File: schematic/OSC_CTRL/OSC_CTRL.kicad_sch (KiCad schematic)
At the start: 14 parts, among them SW1 SW_DIP_x08, SW2 SW_DIP_x08, U1 4052, U2 74AHC595

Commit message: sending ACM v1 rev 1 and APM v5 rev 1 out
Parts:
- removed RV1, RV2, RV3, RV4: R_Potentiometer, Potentiometer_THT:Potentiometer_Bourns_PTA4543_Single_Slide, symbol Device:R_Potentiometer
- removed RV5: 250k, Potentiometer_THT:Potentiometer_Piher_T-16H_Single_Horizontal, symbol Device:R_Potentiometer
- removed SW1: SW_DIP_x08, symbol Switch:SW_DIP_x08
- added D1: 1N5819, Diode_THT:D_DO-41_SOD81_P10.16mm_Horizontal, symbol Diode:1N5819
- added RV11, RV12, RV13, RV14: 10K, Potentiometer_THT:Potentiometer_Bourns_PTA4543_Single_Slide, symbol Device:R_Potentiometer
- added RV15: 250K, Potentiometer_THT:Potentiometer_Piher_T-16H_Single_Horizontal, symbol Device:R_Potentiometer
- added SW3: SW_DIP_x08, symbol Switch:SW_DIP_x08
- RV6, RV7, RV8, RV9: value R_Potentiometer -> 10K
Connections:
- net 3V3: now also RV10.1, RV6.1, RV7.1, RV8.1, RV9.1, RV11.1, RV12.1, RV13.1, RV14.1, RV15.1
- net GND: now also RV10.3, RV6.3, RV7.3, RV8.3, RV9.3, RV11.3, RV12.3, RV13.3, RV14.3, RV15.3
- net OSC1_WAVE0: now also SW3.1
- net OSC1_WAVE1: now also SW3.2
- net OSC1_WAVE2: now also SW3.3
- net OSC_1_ATK: now also RV11.2
- net OSC_1_DEC: now also RV12.2
- net OSC_1_REL: now also U1.15 (X2), RV14.2; no longer U1.11 (X3)
- net OSC_1_SUS: now also U1.11 (X3), RV13.2; no longer U1.15 (X2)
- net OSC_2_ATK: now also RV6.2
- net OSC_2_DEC: now also RV7.2
- net OSC_2_REL: now also RV9.2, U1.2 (Y2); no longer U1.4 (Y3)
- net OSC_2_SUS: now also RV8.2, U1.4 (Y3); no longer U1.2 (Y2)
- net STM32_ADC_15: now also RV15.2
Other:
- note added: "OSCILLATOR 1"
- note added: "OSCILLATOR 2"
- note added: "WAVEFORM SELECT"
- note removed: "OSCILLATOR A"
- note removed: "OSCILLATOR B"
- moved on the sheet: RV10, RV6, RV7, RV8, RV9, SW2, U1, U2

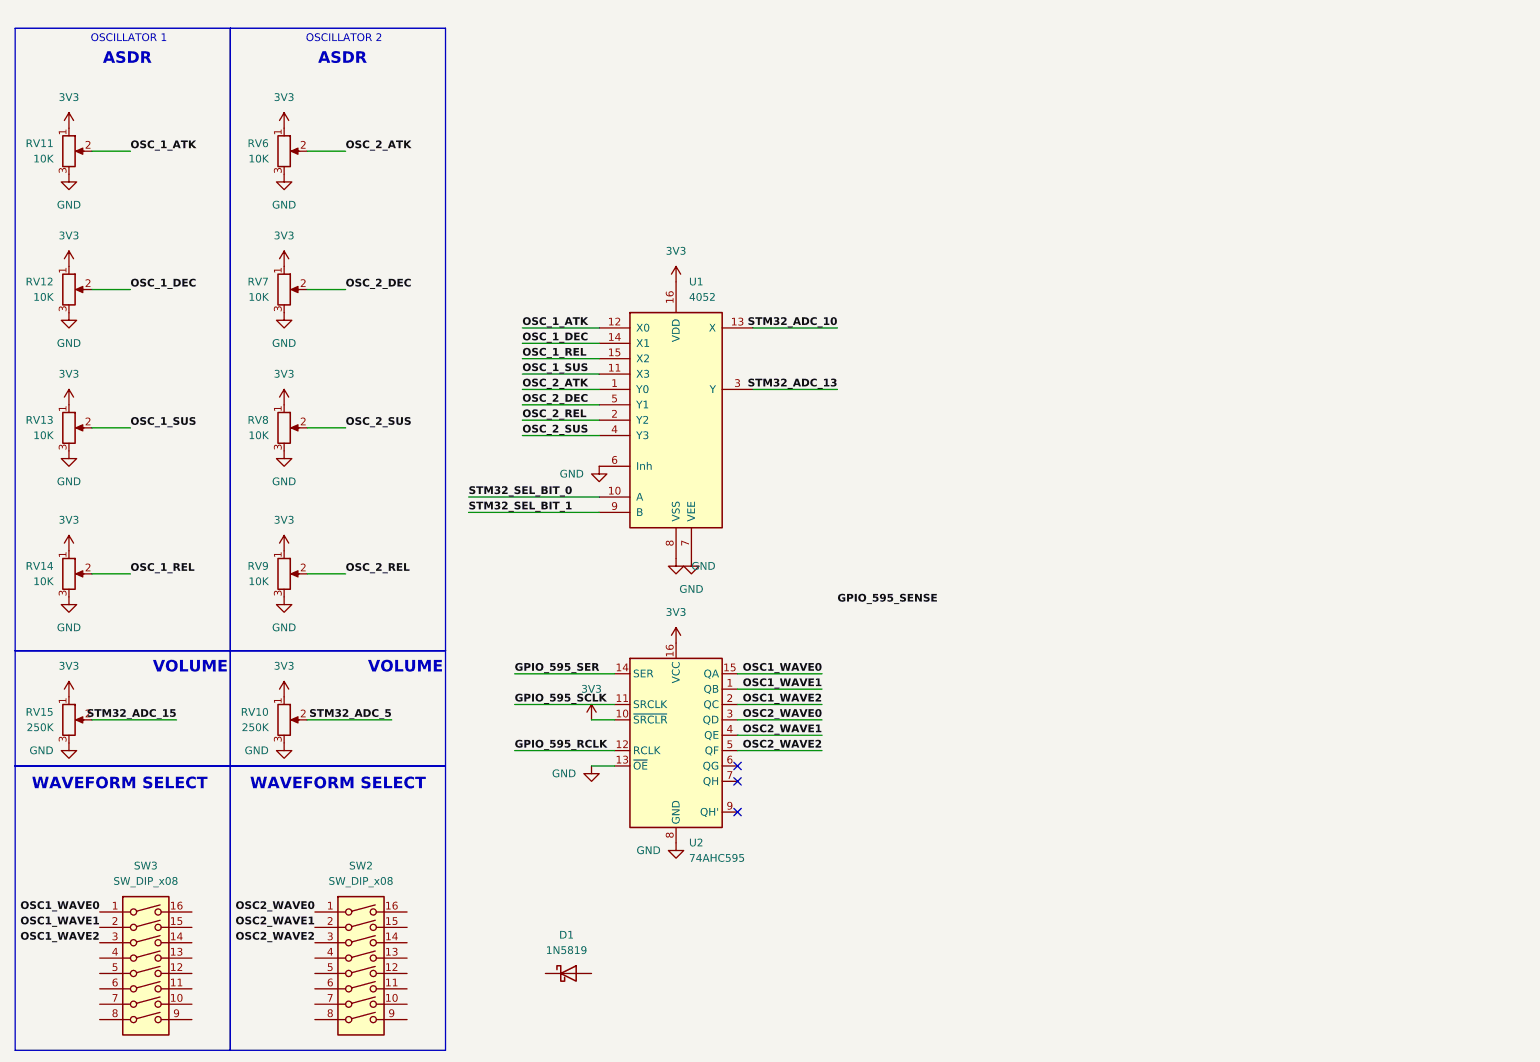
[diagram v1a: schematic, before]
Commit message: starting pcb for oscillator ctrl board
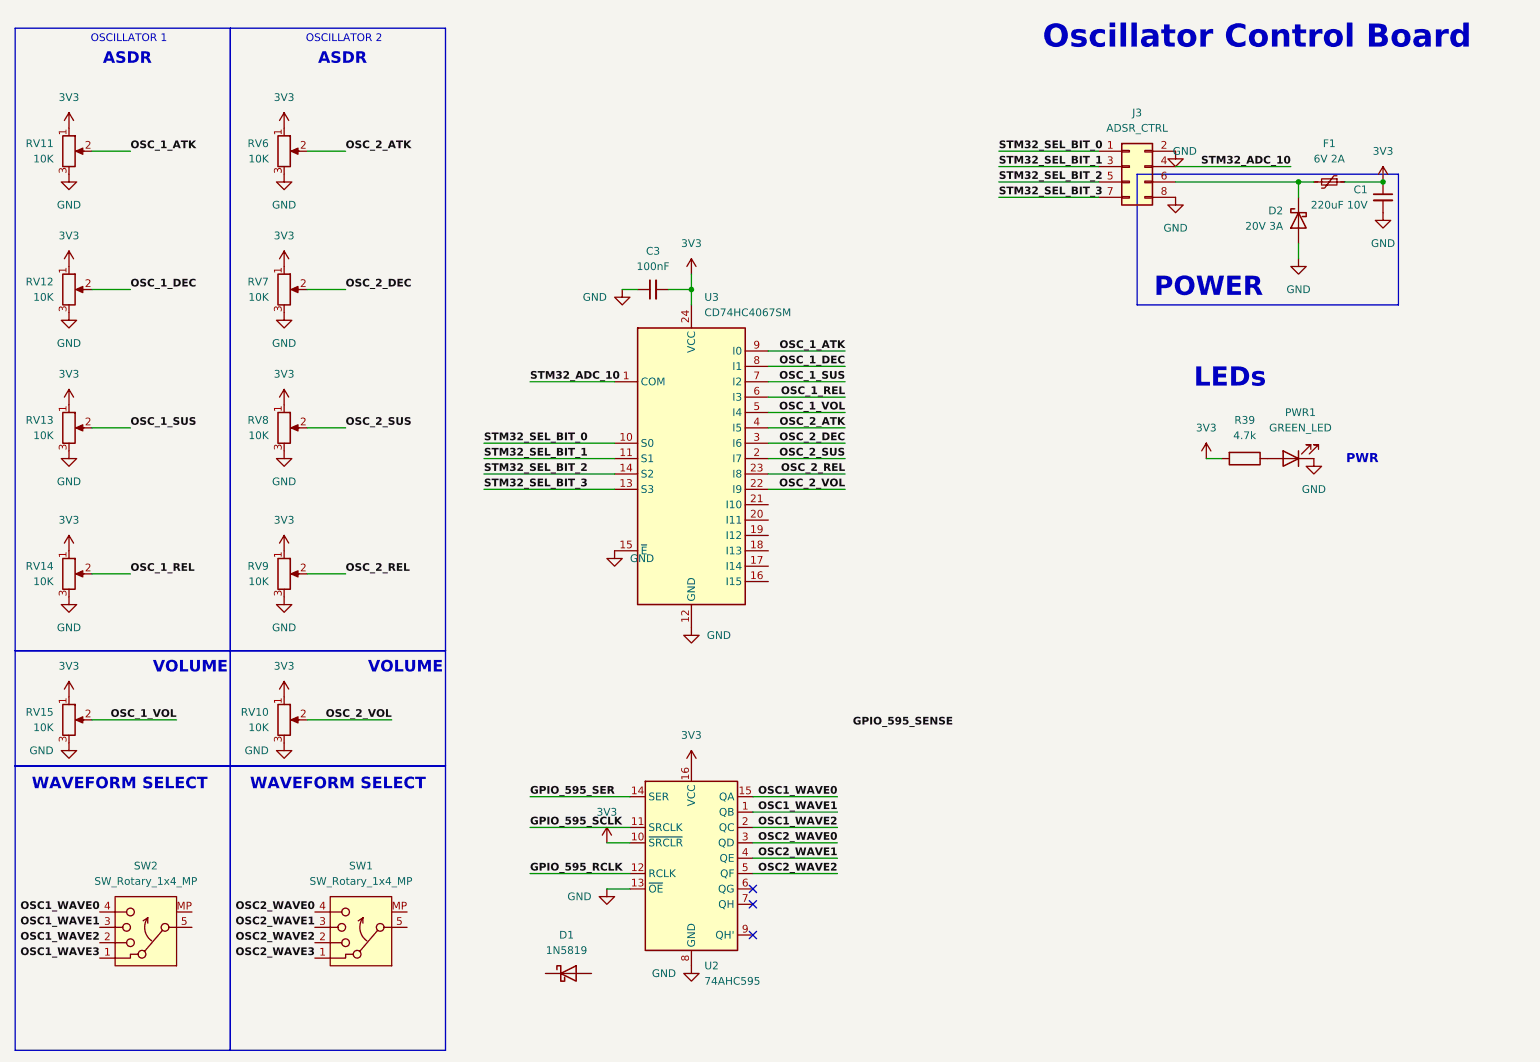
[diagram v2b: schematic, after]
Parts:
- removed SW2, SW3: SW_DIP_x08, symbol Switch:SW_DIP_x08
- removed U1: 4052, symbol 4xxx:4052
- added C1: 220uF 10V, Capacitor_SMD:CP_Elec_4x3, symbol Device:C_Small
- added C3: 100nF, Capacitor_SMD:C_0402_1005Metric, symbol Device:C_Small
- added D2: 20V 3A, Diode_SMD:D_SOD-123, symbol Device:D_Schottky
- added F1: 6V 2A, Fuse:Fuse_0603_1608Metric, symbol Device:Polyfuse_Small
- added J3: ADSR_CTRL, Connector_PinHeader_2.54mm:PinHeader_2x04_P2.54mm_Vertical_SMD, symbol Connector_Generic:Conn_02x04_Odd_Even
- added PWR1: GREEN_LED, LED_SMD:LED_0603_1608Metric, symbol Device:LED
- added R39: 4.7k, Resistor_SMD:R_0201_0603Metric, symbol Device:R
- added SW1, SW2: SW_Rotary_1x4_MP, symbol Switch:SW_Rotary_1x4_MP
- added U3: CD74HC4067SM, Package_SO:SSOP-24_5.3x8.2mm_P0.65mm, symbol 74xx:CD74HC4067SM
- RV10, RV15: value 250K -> 10K
- U2: footprint (none) -> Package_DIP:DIP-16_W7.62mm_SMDSocket_SmallPads
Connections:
- net 3V3: now also C1.1, C3.2, F1.1, R39.2, U3.24 (VCC)
- net GND: now also C1.2, C3.1, D2.2 (A), J3.2 (Pin_2), J3.8 (Pin_8), PWR1.1 (K), U3.12 (GND), U3.15 (~{E})
- net OSC1_WAVE0: now also SW2.4
- net OSC1_WAVE1: now also SW2.3
- net OSC1_WAVE2: now also SW2.2
- net OSC2_WAVE0: now also SW1.4
- net OSC2_WAVE1: now also SW1.3
- net OSC2_WAVE2: now also SW1.2
- net OSC_1_ATK: now also U3.9 (I0)
- net OSC_1_DEC: now also U3.8 (I1)
- net OSC_1_REL: now also U3.6 (I3)
- net OSC_1_SUS: now also U3.7 (I2)
- net OSC_2_ATK: now also U3.4 (I5)
- net OSC_2_DEC: now also U3.3 (I6)
- net OSC_2_REL: now also U3.23 (I8)
- net OSC_2_SUS: now also U3.2 (I7)
- net STM32_ADC_10: now also J3.4 (Pin_4), U3.1 (COM)
- net STM32_SEL_BIT_0: now also J3.1 (Pin_1), U3.10 (S0)
- net STM32_SEL_BIT_1: now also J3.3 (Pin_3), U3.11 (S1)
- net STM32_ADC_15 renamed OSC_1_VOL
- net OSC_1_VOL: now also U3.5 (I4)
- net STM32_ADC_5 renamed OSC_2_VOL
- net OSC_2_VOL: now also U3.22 (I9)
- new net: D2.1 (K), F1.2, J3.6 (Pin_6)
- new net: PWR1.2 (A), R39.1
- new net OSC1_WAVE3: SW2.1
- new net OSC2_WAVE3: SW1.1
- new net STM32_SEL_BIT_2: J3.5 (Pin_5), U3.14 (S2)
- new net STM32_SEL_BIT_3: J3.7 (Pin_7), U3.13 (S3)
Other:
- note added: "LEDs"
- note added: "Oscillator Control Board"
- note added: "POWER"
- note added: "PWR"
- moved on the sheet: U2

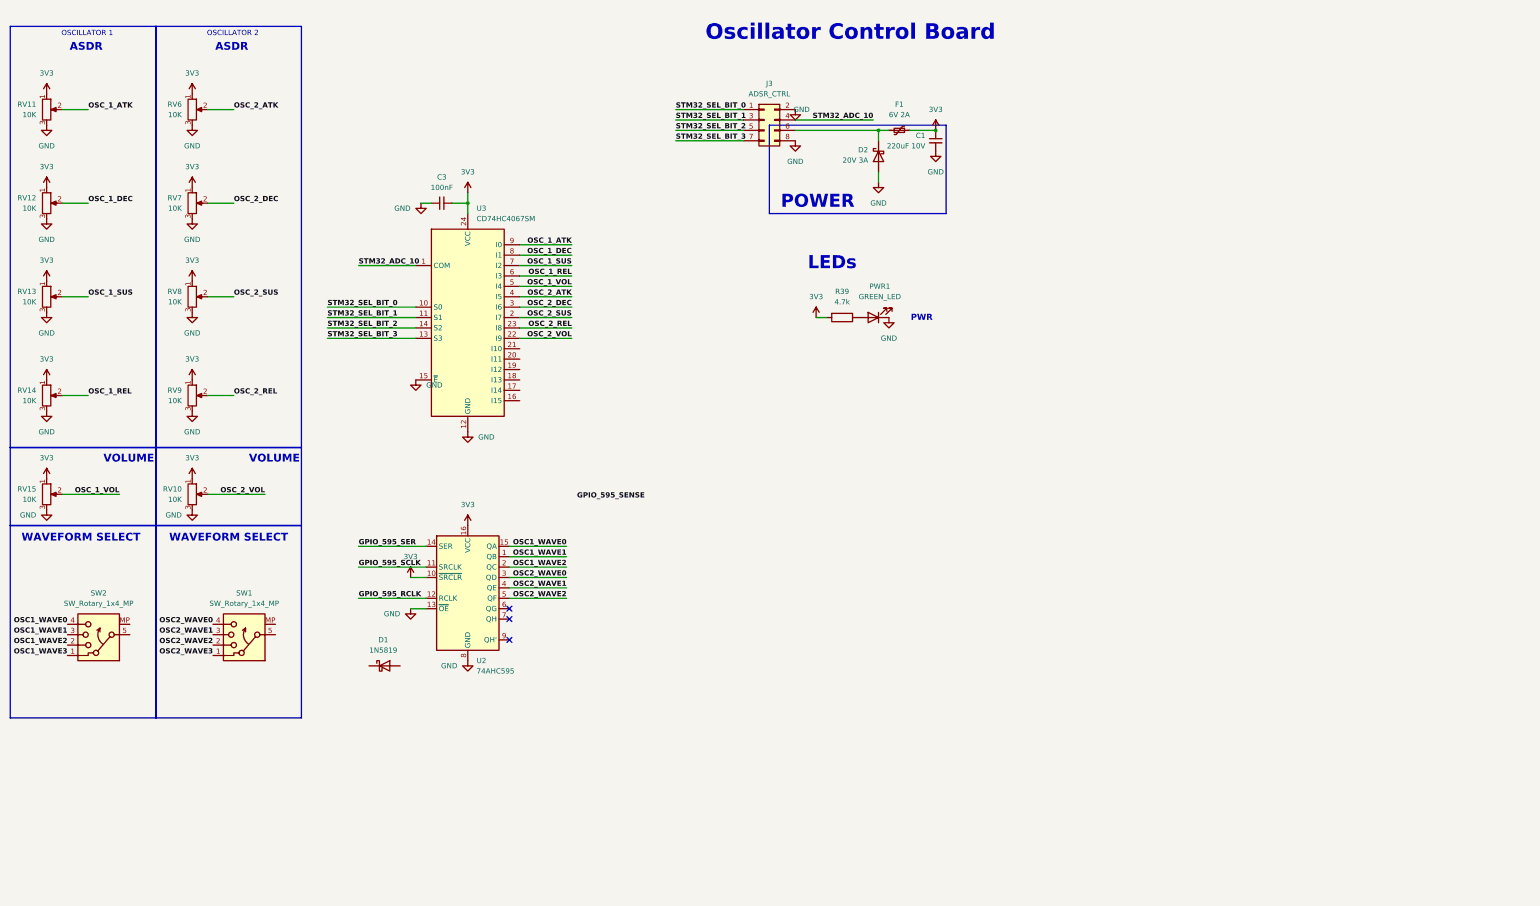
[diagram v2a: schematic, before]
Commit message: oscillator control board sent out
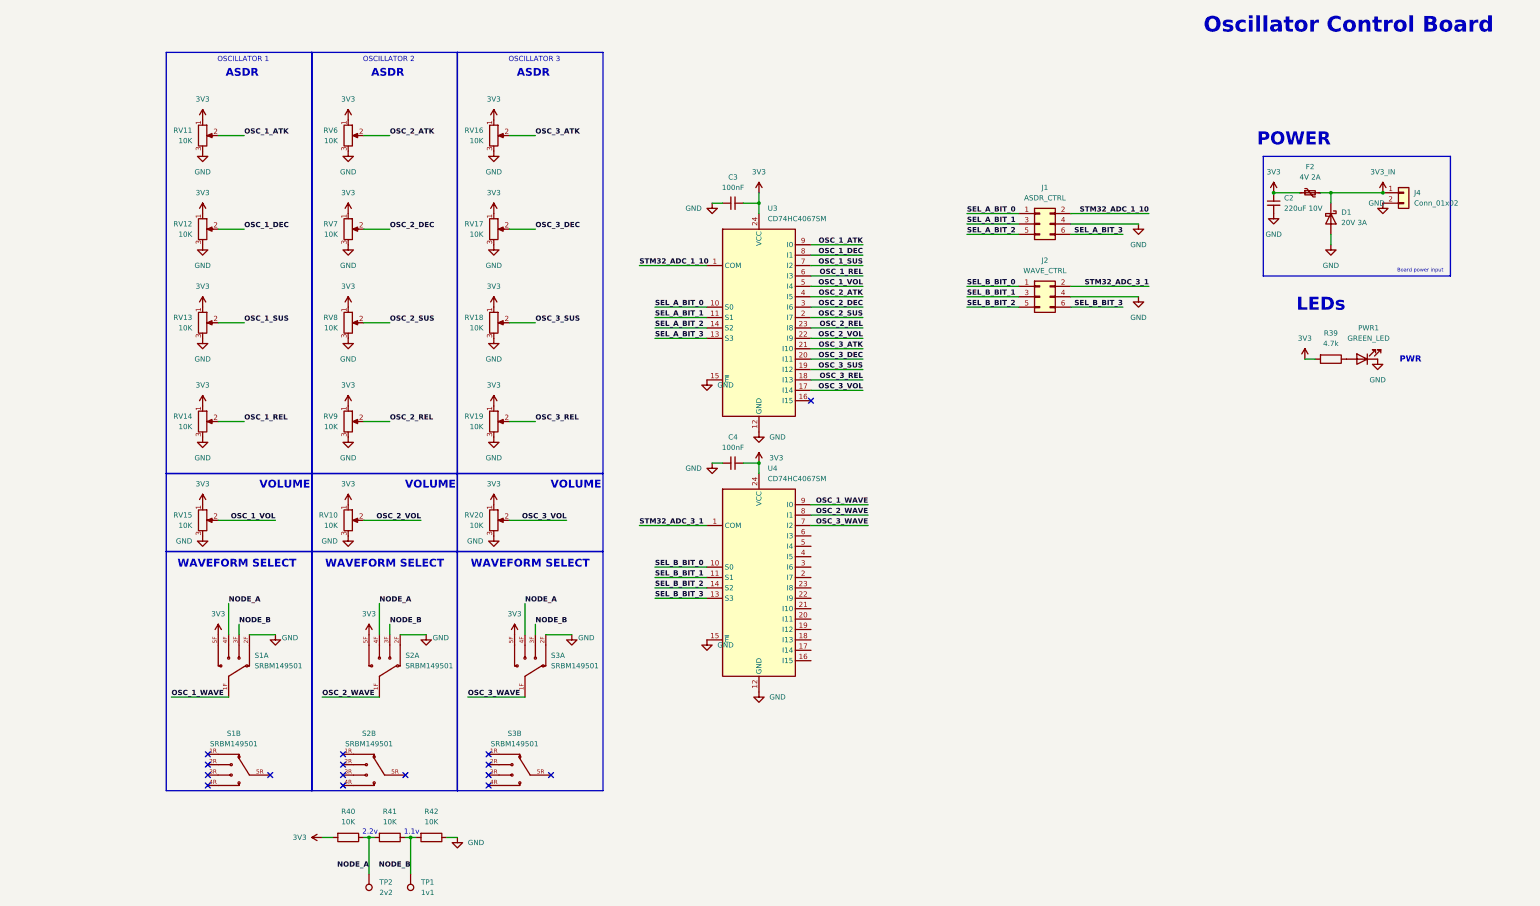
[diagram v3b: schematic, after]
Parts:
- removed C1: 220uF 10V, Capacitor_SMD:CP_Elec_4x3, symbol Device:C_Small
- removed D1: 1N5819, Diode_THT:D_DO-41_SOD81_P10.16mm_Horizontal, symbol Diode:1N5819
- removed D2: 20V 3A, Diode_SMD:D_SOD-123, symbol Device:D_Schottky
- removed F1: 6V 2A, Fuse:Fuse_0603_1608Metric, symbol Device:Polyfuse_Small
- removed J3: ADSR_CTRL, Connector_PinHeader_2.54mm:PinHeader_2x04_P2.54mm_Vertical_SMD, symbol Connector_Generic:Conn_02x04_Odd_Even
- removed SW1, SW2: SW_Rotary_1x4_MP, symbol Switch:SW_Rotary_1x4_MP
- removed U2: 74AHC595, Package_DIP:DIP-16_W7.62mm_SMDSocket_SmallPads, symbol 74xx:74AHC595
- added C2: 220uF 10V, Capacitor_SMD:CP_Elec_4x3, symbol Device:C_Small
- added C4: 100nF, Capacitor_SMD:C_0402_1005Metric, symbol Device:C_Small
- added D1: 20V 3A, Diode_SMD:D_SOD-123, symbol Device:D_Schottky
- added F2: 4V 2A, Fuse:Fuse_0603_1608Metric, symbol Device:Polyfuse_Small
- added J1: ASDR_CTRL, Connector_PinHeader_2.54mm:PinHeader_2x03_P2.54mm_Vertical_SMD, symbol Connector_Generic:Conn_02x03_Odd_Even
- added J2: WAVE_CTRL, Connector_PinHeader_2.54mm:PinHeader_2x03_P2.54mm_Vertical_SMD, symbol Connector_Generic:Conn_02x03_Odd_Even
- added J4: Conn_01x02, Connector_PinSocket_2.54mm:PinSocket_1x02_P2.54mm_Vertical_SMD_Pin1Left, symbol Connector_Generic:Conn_01x02
- added R40, R41, R42: 10K, Resistor_SMD:R_0201_0603Metric, symbol Device:R
- added RV16, RV17, RV18, RV19: 10K, my_footprints:Potentiometer_Bourns_PTA4543_Single_Slide, symbol Device:R_Potentiometer
- added RV20: 10K, my_footprints:Potentiometer_Piher_PC-16_Single_Horizontal, symbol Device:R_Potentiometer
- added S1, S2, S3: SRBM149501, my_footprints:SW_SRBM149501, symbol SRBM149501:SRBM149501
- added TP1: 1v1, TestPoint:TestPoint_Pad_D1.0mm, symbol Connector:TestPoint
- added TP2: 2v2, TestPoint:TestPoint_Pad_D1.0mm, symbol Connector:TestPoint
- added U4: CD74HC4067SM, Package_SO:SSOP-24_5.3x8.2mm_P0.65mm, symbol 74xx:CD74HC4067SM
- RV10: footprint Potentiometer_THT:Potentiometer_Piher_T-16H_Single_Horizontal -> my_footprints:Potentiometer_Piher_PC-16_Single_Horizontal
- RV11, RV12, RV13, RV14, RV6, RV7, RV8, RV9: footprint Potentiometer_THT:Potentiometer_Bourns_PTA4543_Single_Slide -> my_footprints:Potentiometer_Bourns_PTA4543_Single_Slide
- RV15: footprint Potentiometer_THT:Potentiometer_Piher_T-16H_Single_Horizontal -> Potentiometer_THT:Potentiometer_Piher_PC-16_Single_Horizontal
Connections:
- net 3V3: now also C2.1, C4.2, F2.1, R40.2, RV16.1, RV17.1, RV18.1, RV19.1, RV20.1, S1.5F, S2.5F, S3.5F, U4.24 (VCC)
- net GND: now also C2.2, C4.1, D1.2 (A), J1.4 (Pin_4), J2.4 (Pin_4), J4.2 (Pin_2), R42.1, RV16.3, RV17.3, RV18.3, RV19.3, RV20.3, S1.2F, S2.2F, S3.2F, U4.12 (GND), U4.15 (~{E})
- net OSC_3_VOL: now reaches U3.17 (I14)
- net OSC_3_VOL: now also RV20.2
- net OSC_3_REL: now reaches U3.18 (I13)
- net OSC_3_REL: now also RV19.2
- net OSC_3_SUS: now reaches U3.19 (I12)
- net OSC_3_SUS: now also RV18.2
- net OSC_3_DEC: now reaches U3.20 (I11)
- net OSC_3_DEC: now also RV17.2
- net OSC_3_ATK: now reaches U3.21 (I10)
- net OSC_3_ATK: now also RV16.2
- net STM32_ADC_10 renamed STM32_ADC_1_10
- net STM32_ADC_1_10: now also J1.2 (Pin_2)
- net STM32_SEL_BIT_0 renamed SEL_A_BIT_0
- net SEL_A_BIT_0: now also J1.1 (Pin_1)
- net STM32_SEL_BIT_1 renamed SEL_A_BIT_1
- net SEL_A_BIT_1: now also J1.3 (Pin_3)
- net STM32_SEL_BIT_2 renamed SEL_A_BIT_2
- net SEL_A_BIT_2: now also J1.5 (Pin_5)
- net STM32_SEL_BIT_3 renamed SEL_A_BIT_3
- net SEL_A_BIT_3: now also J1.6 (Pin_6)
- new net 3V3_IN: D1.1 (K), F2.2, J4.1 (Pin_1)
- new net NODE_A: R40.1, R41.2, S1.4F, S2.4F, S3.4F, TP2.1
- new net NODE_B: R41.1, R42.2, S1.3F, S2.3F, S3.3F, TP1.1
- new net OSC_1_WAVE: S1.1F, U4.9 (I0)
- new net OSC_2_WAVE: S2.1F, U4.8 (I1)
- new net OSC_3_WAVE: S3.1F, U4.7 (I2)
- new net SEL_B_BIT_0: J2.1 (Pin_1), U4.10 (S0)
- new net SEL_B_BIT_1: J2.3 (Pin_3), U4.11 (S1)
- new net SEL_B_BIT_2: J2.5 (Pin_5), U4.14 (S2)
- new net SEL_B_BIT_3: J2.6 (Pin_6), U4.13 (S3)
- new net STM32_ADC_3_1: J2.2 (Pin_2), U4.1 (COM)
- no-connect marks 3 -> 16
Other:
- note added: "1.1v"
- note added: "2.2v"
- note added: "Board power input"
- note added: "OSCILLATOR 3"
- moved on the sheet: C3, PWR1, R39, RV10, RV11, RV12, RV13, RV14, RV15, RV6, RV7, RV8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

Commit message: getting the boards fabbed
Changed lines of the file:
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@@
 	(wire
 		(pts
-			(xy 200.66 156.21) (xy 213.36 156.21)
+			(xy 196.85 156.21) (xy 213.36 156.21)
 		)
 		(stroke
@@
 	(wire
 		(pts
-			(xy 200.66 151.13) (xy 213.36 151.13)
+			(xy 196.85 151.13) (xy 213.36 151.13)
 		)
 		(stroke
@@
 	(wire
 		(pts
-			(xy 200.66 148.59) (xy 213.36 148.59)
+			(xy 196.85 148.59) (xy 213.36 148.59)
 		)
 		(stroke
@@
 	(wire
 		(pts
-			(xy 200.66 153.67) (xy 213.36 153.67)
+			(xy 196.85 153.67) (xy 213.36 153.67)
 		)
 		(stroke
@@
 	)
 	(label "SEL_B_BIT_3"
-		(at 200.66 156.21 0)
+		(at 196.85 156.21 0)
 		(effects
 			(font
@@
 	)
 	(label "SEL_B_BIT_1"
-		(at 200.66 151.13 0)
+		(at 196.85 151.13 0)
 		(effects
 			(font
@@
 	)
 	(label "SEL_B_BIT_2"
-		(at 200.66 153.67 0)
+		(at 196.85 153.67 0)
 		(effects
 			(font
@@
 	)
 	(label "SEL_B_BIT_0"
-		(at 200.66 148.59 0)
-		(effects
-			(font
+		(at 196.85 148.59 0)
+		(effects
+			(font
